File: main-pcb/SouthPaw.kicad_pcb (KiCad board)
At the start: 2 copper layers, 95.5 x 130.5 mm, 68 parts, among them SW1 SW_Push, SW10 SW_Push, SW11 SW_Push, SW12 SW_Push, SW13 SW_Push, SW14 SW_Push, SW15 SW_Push, SW16 SW_Push, SW17 SW_Push, SW18 SW_Push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

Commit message: Making progress
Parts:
- removed L10, L11, logo1, logo3, logo5, logo6, logo7, logo8: LOGO, LOGO
- added STA10: , , F.Cu at (79.0, 134.4)
- added STA9: , , F.Cu at (79.0, 96.3)
- STA1: value 0.91in 128x32 I2C STEMMA QT standoff only -> 0.91in 128x32 I2C STEMMA QT standoff only with cutout; footprint PeteCB:0.91in 128x32 I2C STEMMA QT standoff only -> PeteCB:0.91in 128x32 I2C STEMMA QT standoff only with cutout
- U1: footprint PeteCB:KB2040 through hole hybrid (modified from Elite-C-castellated-24pin-holes) -> PeteCB:KB2040 through hole only (top mount with hotpins 3d model view)
- moved STA3 19.1 mm to (40.9, 96.3)
- moved STA5 19.0 mm to (98.0, 115.4)
- moved STA6 14.7 mm to (114.4, 53.0)
- moved STA7 4.61 mm to (25.4, 54.0)
- moved U1 4.12 mm to (100.7, 39.0), turned to -135 degrees
- moved D3 2.93 mm to (40.8, 41.5)
- moved D8 2.93 mm to (61.6, 41.7)
- moved D4 2.93 mm to (40.8, 31.6)
- moved D6 2.93 mm to (52.2, 26.5)
- moved D9 2.93 mm to (61.6, 31.7)
- moved D1 2.93 mm to (29.1, 26.5)
- moved D10 2.93 mm to (59.1, 31.7)
- moved D2 2.93 mm to (38.3, 41.5)
- moved D5 2.93 mm to (38.3, 31.6)
- moved D7 2.93 mm to (59.1, 41.6)
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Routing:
- net /GND: track 27.6 -> 620.6 mm, vias 21 -> 1
- net /3.3V: track 777.4 -> 498.9 mm, vias 11 -> 6
- net Net-(D5-Pad1): track 118.8 -> 219.7 mm, vias 0 -> 5
- net Net-(RSW1-PadS2): track 150.0 -> 186.0 mm, vias 0 -> 4
- net Net-(D10-Pad2): track 110.9 -> 78.8 mm
- net Net-(SW1-Pad11): track 216.7 -> 184.9 mm, vias 2 -> 1
- net Net-(D25-Pad1): track 155.8 -> 124.0 mm
- net Net-(SW15-Pad22): track 45.4 -> 14.6 mm, vias 1 -> 0
- net Net-(RSW1-PadA): track 124.4 -> 153.0 mm, vias 1 -> 5
- net Net-(D15-Pad1): track 31.0 -> 59.5 mm
- net Net-(D19-Pad1): track 115.3 -> 143.5 mm
- net Net-(RSW1-PadB): track 91.2 -> 118.9 mm, vias 0 -> 2
- net Net-(D8-Pad1): track 77.6 -> 50.5 mm, vias 3 -> 1
- net Net-(SW21-Pad22): track 48.4 -> 22.5 mm, vias 1 -> 0
- net Net-(SW1-Pad24): track 132.4 -> 107.3 mm, vias 4 -> 1
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- removed copper zone on B.Cu, net /GND
- removed copper zone on F.Cu, net /GND
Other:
- board size 95.5 x 130.5 mm -> 99.7 x 136.9 mm
- board text added: "ES 2"

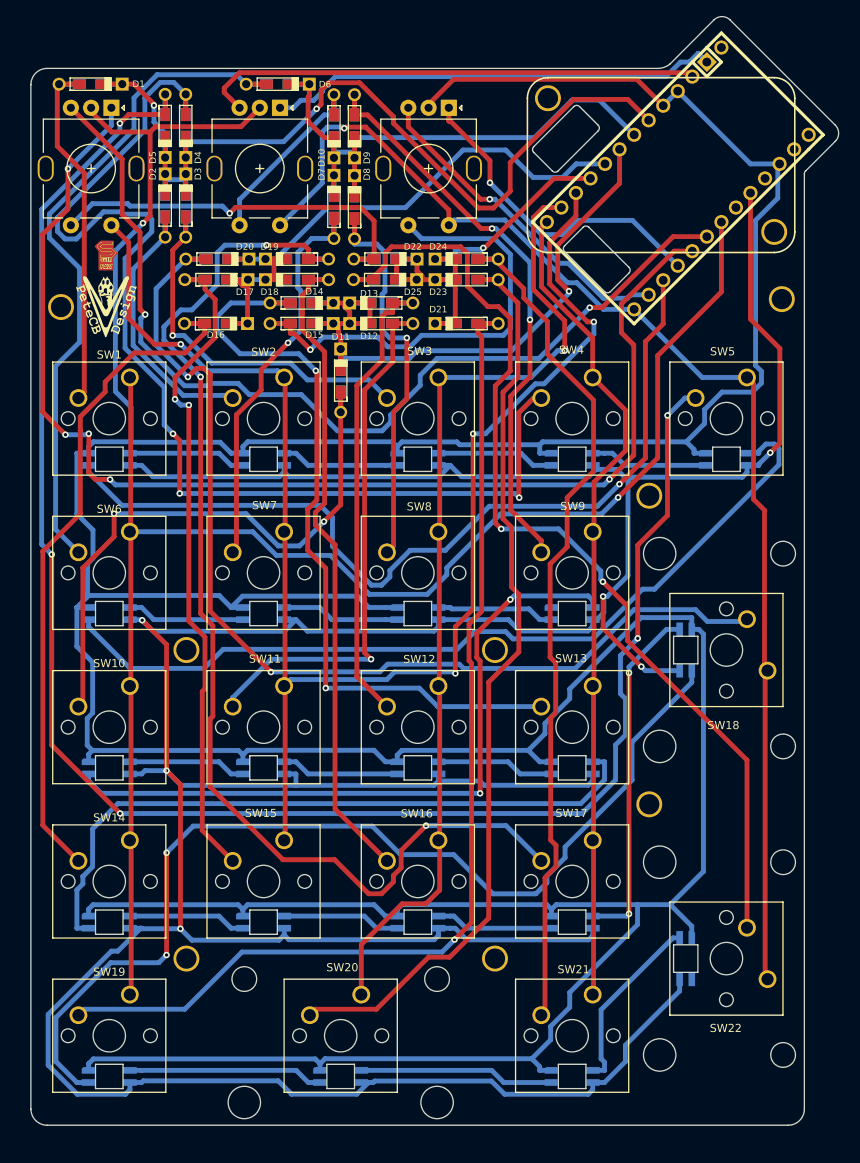
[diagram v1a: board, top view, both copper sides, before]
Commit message: fixed pinnouts
rotary encoders now all share a common a pin
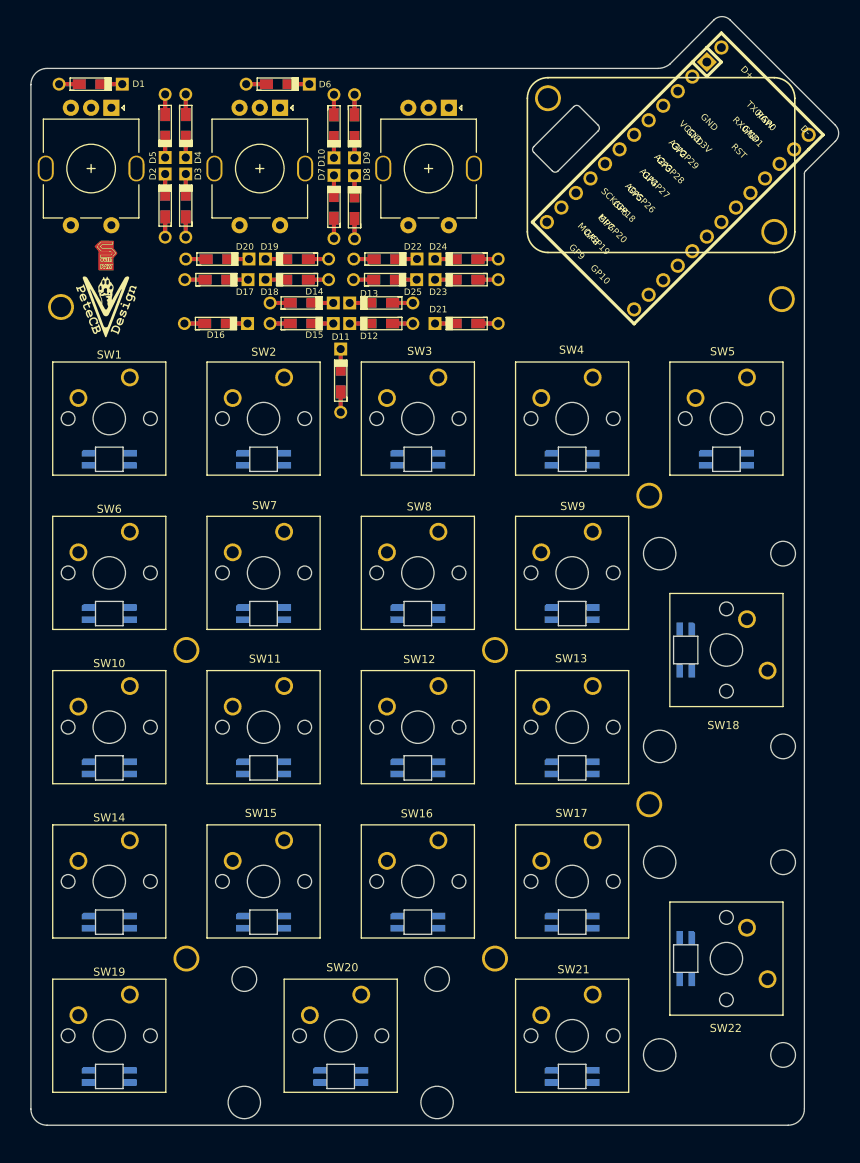
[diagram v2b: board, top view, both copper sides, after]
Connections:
- RSW1 pad A: Net-(RSW1-PadA) -> /ENCA
- RSW2 pad A: Net-(RSW2-PadA) -> /ENCA
- RSW2 pad S2: Net-(RSW2-PadS2) -> Net-(U1-Pad18)
- RSW3 pad A: Net-(RSW3-PadA) -> /ENCA
- RSW3 pad S2: Net-(RSW2-PadS2) -> Net-(U1-Pad18)
- SW1 pad 21: /3.3V -> /RAW
- SW10 pad 21: /3.3V -> /RAW
- SW11 pad 21: /3.3V -> /RAW
- SW12 pad 21: /3.3V -> /RAW
- SW13 pad 21: /3.3V -> /RAW
- SW14 pad 21: /3.3V -> /RAW
- SW15 pad 21: /3.3V -> /RAW
- SW16 pad 21: /3.3V -> /RAW
- SW17 pad 21: /3.3V -> /RAW
- SW18 pad 11: Net-(RSW2-PadS2) -> Net-(U1-Pad18)
- SW18 pad 21: /3.3V -> /RAW
- SW19 pad 21: /3.3V -> /RAW
- SW2 pad 21: /3.3V -> /RAW
- SW20 pad 21: /3.3V -> /RAW
- SW21 pad 21: /3.3V -> /RAW
- SW22 pad 11: Net-(RSW2-PadS2) -> Net-(U1-Pad18)
- SW22 pad 21: /3.3V -> /RAW
- SW3 pad 21: /3.3V -> /RAW
- SW4 pad 21: /3.3V -> /RAW
- SW5 pad 11: Net-(RSW2-PadS2) -> Net-(U1-Pad18)
- SW5 pad 21: /3.3V -> /RAW
- SW6 pad 21: /3.3V -> /RAW
- SW7 pad 21: /3.3V -> /RAW
- SW8 pad 21: /3.3V -> /RAW
- SW9 pad 21: /3.3V -> /RAW
- U1 pad 0: (no net) -> unconnected-(U1-Pad0)
- U1 pad 1: Net-(RSW2-PadA) -> Net-(RSW2-PadB)
- U1 pad 13: Net-(RSW2-PadS2) -> /ENCA
- U1 pad 14: Net-(RSW3-PadB) -> Net-(SW1-Pad24)
- U1 pad 15: Net-(SW1-Pad24) -> unconnected-(U1-Pad15)
- U1 pad 16: Net-(RSW3-PadA) -> unconnected-(U1-Pad16)
- U1 pad 17: Net-(RSW1-PadA) -> unconnected-(U1-Pad17)
- U1 pad 18: Net-(RSW1-PadB) -> Net-(U1-Pad18)
- U1 pad 2: Net-(RSW2-PadB) -> Net-(RSW3-PadB)
- U1 pad 20: unconnected-(U1-Pad20) -> Net-(RSW1-PadB)
- U1 pad 24: unconnected-(U1-Pad24) -> /RAW
- U1 pad 25: (no net) -> unconnected-(U1-Pad25)
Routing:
- net /GND: track 620.6 -> 0.00 mm, vias 1 -> 0
- net /3.3V: track 498.9 -> 0.00 mm, vias 6 -> 0
- net Net-(D5-Pad1): track 219.7 -> 0.00 mm, vias 5 -> 0
- net Net-(RSW1-PadS2): track 186.0 -> 0.00 mm, vias 4 -> 0
- net Net-(SW1-Pad11): track 184.9 -> 0.00 mm, vias 1 -> 0
- net Net-(RSW2-PadS2): track 156.5 -> 0.00 mm, vias 1 -> 0
- net Net-(RSW1-PadA): track 153.0 -> 0.00 mm, vias 5 -> 0
- net Net-(D19-Pad1): track 143.5 -> 0.00 mm, vias 3 -> 0
- net Net-(D4-Pad1): track 140.4 -> 0.00 mm, vias 3 -> 0
- net Net-(D21-Pad1): track 133.5 -> 0.00 mm, vias 1 -> 0
- net Net-(D20-Pad1): track 129.2 -> 0.00 mm, vias 2 -> 0
- net Net-(SW18-Pad22): track 126.0 -> 0.00 mm, vias 2 -> 0
- net Net-(D25-Pad1): track 124.0 -> 0.00 mm, vias 2 -> 0
- net Net-(SW12-Pad11): track 121.3 -> 0.00 mm, vias 1 -> 0
- net Net-(RSW1-PadB): track 118.9 -> 0.00 mm, vias 2 -> 0
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
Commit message: Some work on traces (drc errors present)
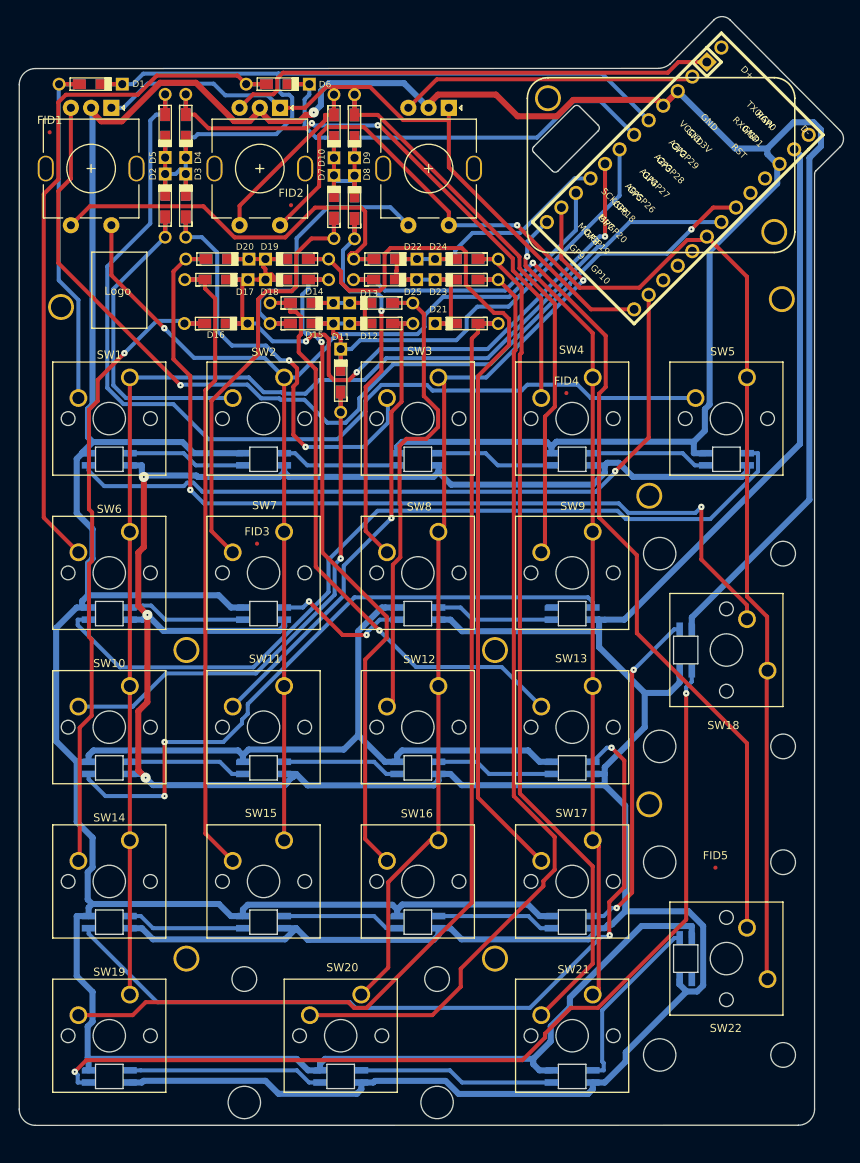
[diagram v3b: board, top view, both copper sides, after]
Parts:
- removed logo0, logo4: LOGO, LOGO
- added FID1: Fiducial, Fiducial:Fiducial_0.5mm_Mask1mm, F.Cu at (24.0, 32.4)
- added FID2: Fiducial, Fiducial:Fiducial_0.5mm_Mask1mm, F.Cu at (53.8, 41.4)
- added FID3: Fiducial, Fiducial:Fiducial_0.5mm_Mask1mm, F.Cu at (49.6, 83.2)
- added FID4: Fiducial, Fiducial:Fiducial_0.5mm_Mask1mm, F.Cu at (87.8, 64.6)
- added FID5: Fiducial, Fiducial:Fiducial_0.5mm_Mask1mm, F.Cu at (106.2, 123.2)
- H1: renamed from STA1; value 0.91in 128x32 I2C STEMMA QT standoff only with cutout -> MountingHole
- H2: renamed from STA7; value (none) -> MountingHole; footprint (none) -> PeteCB:m2.5 hole
- H3: renamed from STA6; value (none) -> MountingHole; footprint (none) -> PeteCB:m2.5 hole
- H4: renamed from STA2; value m2.5 hole -> MountingHole
- H5: renamed from STA3; value (none) -> MountingHole; footprint (none) -> PeteCB:m2.5 hole
- H6: renamed from STA9; value (none) -> MountingHole; footprint (none) -> PeteCB:m2.5 hole
- H7: renamed from STA5; value (none) -> MountingHole; footprint (none) -> PeteCB:m2.5 hole
- H8: renamed from STA4; value (none) -> MountingHole; footprint (none) -> PeteCB:m2.5 hole
- H9: renamed from STA10; value (none) -> MountingHole; footprint (none) -> PeteCB:m2.5 hole
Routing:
- net /GND: track 0.00 -> 662.8 mm, vias 0 -> 1
- net /RAW: track 0.00 -> 517.8 mm, vias 0 -> 3
- net Net-(U1-Pad18): track 0.00 -> 168.1 mm, vias 0 -> 1
- net Net-(SW1-Pad11): track 0.00 -> 158.9 mm
- net Net-(RSW1-PadS2): track 0.00 -> 139.1 mm, vias 0 -> 1
- net Net-(D21-Pad1): track 0.00 -> 131.7 mm
- net Net-(RSW1-PadB): track 0.00 -> 123.6 mm, vias 0 -> 2
- net Net-(D5-Pad1): track 0.00 -> 122.4 mm
- net Net-(D1-Pad2): track 0.00 -> 120.6 mm
- net Net-(D25-Pad1): track 0.00 -> 120.3 mm, vias 0 -> 1
- net Net-(D23-Pad1): track 0.00 -> 120.3 mm
- net Net-(SW18-Pad22): track 0.00 -> 117.4 mm, vias 0 -> 2
- net Net-(D20-Pad1): track 0.00 -> 115.8 mm, vias 0 -> 2
- net Net-(SW12-Pad11): track 0.00 -> 114.3 mm, vias 0 -> 1
- net Net-(D19-Pad1): track 0.00 -> 111.9 mm
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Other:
- board size 99.7 x 136.9 mm -> 101.8 x 136.9 mm
- board text added: "Logo"

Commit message: fixed schematic errors
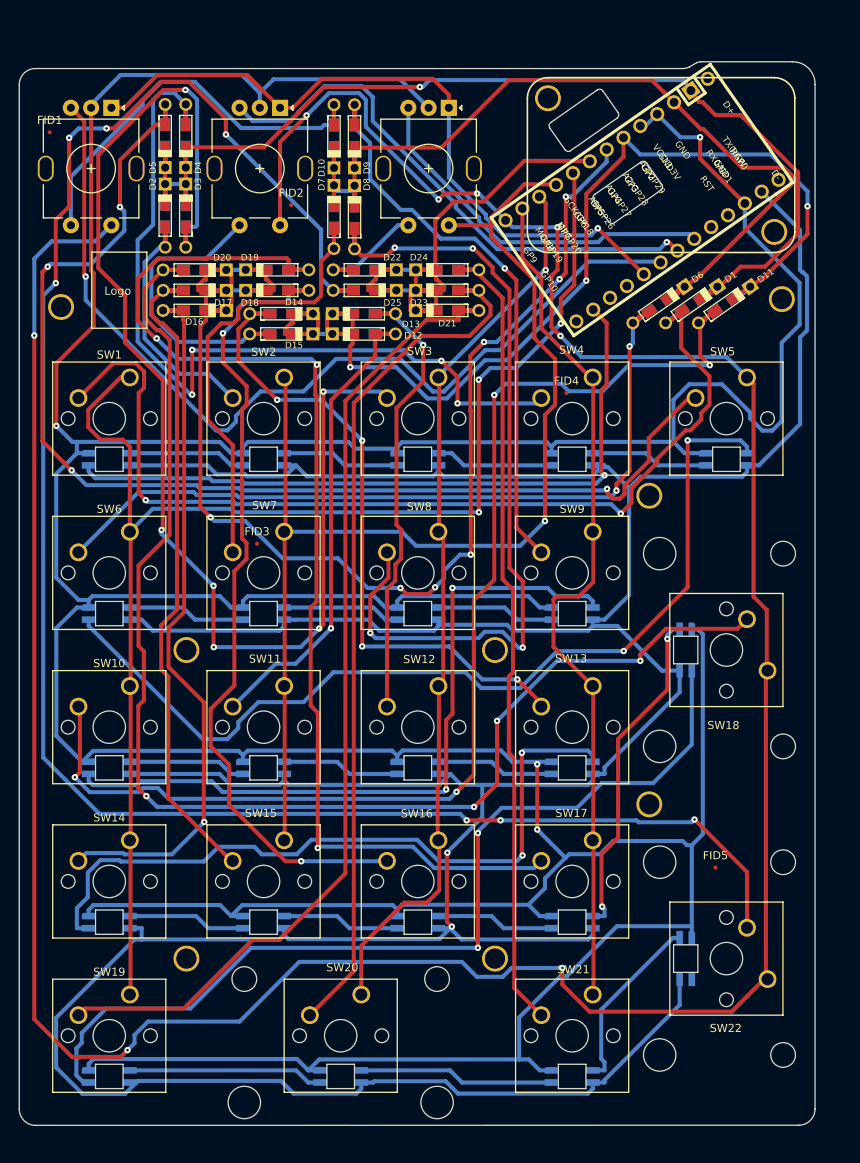
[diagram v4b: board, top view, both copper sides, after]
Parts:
- moved D1 79.0 mm to (103.2, 53.7), turned to 35 degrees
- moved D6 54.4 mm to (99.2, 53.7), turned to 35 degrees
- moved D11 48.3 mm to (107.3, 53.7), turned to 35 degrees
- moved U1 5.19 mm to (96.1, 41.5), turned to -145 degrees
- moved D20 3.11 mm to (41.9, 49.4)
- moved D16 3.09 mm to (41.9, 54.4)
- moved D17 2.99 mm to (41.9, 51.9)
- moved D21 2.88 mm to (73.1, 54.4)
- moved D22 2.88 mm to (62.9, 49.4)
- moved D25 2.84 mm to (62.9, 51.9)
- moved D14 2.84 mm to (52.6, 54.8)
- moved D15 2.82 mm to (52.6, 57.3)
- moved D18 2.78 mm to (52.1, 51.9)
- moved D19 2.78 mm to (52.1, 49.4)
- moved D23 2.73 mm to (73.1, 51.9)
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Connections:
- net /3.3V renamed +3.3V
- net /RAW renamed +5V
- net Net-(SW1-Pad24) renamed /ledDriver
- D1 pad 2: Net-(D1-Pad2) -> /Row1
- D10 pad 2: Net-(D10-Pad2) -> /Row2
- D11 pad 2: Net-(D11-Pad2) -> /Row3
- D12 pad 2: Net-(D11-Pad2) -> /Row3
- D13 pad 2: Net-(D11-Pad2) -> /Row3
- D14 pad 2: Net-(D11-Pad2) -> /Row3
- D15 pad 2: Net-(D11-Pad2) -> /Row3
- D16 pad 2: Net-(D16-Pad2) -> /Row4
- D17 pad 2: Net-(D16-Pad2) -> /Row4
- D18 pad 2: Net-(D16-Pad2) -> /Row4
- D19 pad 2: Net-(D16-Pad2) -> /Row4
- D2 pad 2: Net-(D1-Pad2) -> /Row1
- D20 pad 2: Net-(D16-Pad2) -> /Row4
- D21 pad 2: Net-(D21-Pad2) -> /Row5
- D22 pad 2: Net-(D21-Pad2) -> /Row5
- D23 pad 2: Net-(D21-Pad2) -> /Row5
- D24 pad 2: Net-(D21-Pad2) -> /Row5
- D25 pad 2: Net-(D21-Pad2) -> /Row5
- D3 pad 2: Net-(D1-Pad2) -> /Row1
- D4 pad 2: Net-(D1-Pad2) -> /Row1
- D5 pad 2: Net-(D1-Pad2) -> /Row1
- D6 pad 2: Net-(D10-Pad2) -> /Row2
- D7 pad 2: Net-(D10-Pad2) -> /Row2
- D8 pad 2: Net-(D10-Pad2) -> /Row2
- D9 pad 2: Net-(D10-Pad2) -> /Row2
- RSW1 pad B: Net-(RSW1-PadB) -> /ENC1B
- RSW1 pad C: /GND -> GND
- RSW1 pad S1: Net-(D22-Pad1) -> Net-(D10-Pad1)
- RSW1 pad S2: Net-(RSW1-PadS2) -> /ColE
- RSW2 pad B: Net-(RSW2-PadB) -> /ENC2B
- RSW2 pad C: /GND -> GND
- RSW2 pad S1: Net-(D10-Pad1) -> Net-(D15-Pad1)
- RSW2 pad S2: Net-(U1-Pad18) -> /ColE
- RSW3 pad B: Net-(RSW3-PadB) -> /ENC3B
- RSW3 pad C: /GND -> GND
- RSW3 pad S1: Net-(D15-Pad1) -> Net-(D22-Pad1)
- RSW3 pad S2: Net-(U1-Pad18) -> /ColB
- SW1 pad 11: Net-(SW1-Pad11) -> /ColA
- SW1 pad 23: /GND -> GND
- SW10 pad 11: Net-(SW1-Pad11) -> /ColA
- SW10 pad 23: /GND -> GND
- SW11 pad 11: Net-(RSW1-PadS2) -> /ColB
- SW11 pad 23: /GND -> GND
- SW12 pad 11: Net-(SW12-Pad11) -> /ColC
- SW12 pad 23: /GND -> GND
- SW13 pad 11: Net-(SW13-Pad11) -> /ColD
- SW13 pad 23: /GND -> GND
- SW14 pad 11: Net-(SW1-Pad11) -> /ColA
- SW14 pad 23: /GND -> GND
- SW15 pad 11: Net-(RSW1-PadS2) -> /ColB
- SW15 pad 23: /GND -> GND
- SW16 pad 11: Net-(SW12-Pad11) -> /ColC
- SW16 pad 23: /GND -> GND
- SW17 pad 11: Net-(SW13-Pad11) -> /ColD
- SW17 pad 23: /GND -> GND
- SW18 pad 11: Net-(U1-Pad18) -> /ColE
- SW18 pad 23: /GND -> GND
- SW19 pad 11: Net-(SW1-Pad11) -> /ColA
- SW19 pad 23: /GND -> GND
- SW2 pad 11: Net-(RSW1-PadS2) -> /ColB
- SW2 pad 23: /GND -> GND
- SW20 pad 11: Net-(SW12-Pad11) -> /ColC
- SW20 pad 23: /GND -> GND
- SW21 pad 11: Net-(SW13-Pad11) -> /ColD
- SW21 pad 23: /GND -> GND
- SW22 pad 11: Net-(U1-Pad18) -> /ColE
- SW22 pad 23: /GND -> GND
- SW3 pad 11: Net-(SW12-Pad11) -> /ColC
- SW3 pad 23: /GND -> GND
- SW4 pad 11: Net-(SW13-Pad11) -> /ColD
- SW4 pad 23: /GND -> GND
- SW5 pad 11: Net-(U1-Pad18) -> /ColE
- SW5 pad 23: /GND -> GND
- SW6 pad 11: Net-(SW1-Pad11) -> /ColA
- SW6 pad 23: /GND -> GND
- SW7 pad 11: Net-(RSW1-PadS2) -> /ColB
- SW7 pad 23: /GND -> GND
- SW8 pad 11: Net-(SW12-Pad11) -> /ColC
- SW8 pad 23: /GND -> GND
- SW9 pad 11: Net-(SW13-Pad11) -> /ColD
- SW9 pad 23: unconnected-(SW9-Pad23) -> GND
- U1 pad 1: Net-(RSW2-PadB) -> /Row1
- U1 pad 10: Net-(RSW1-PadS2) -> /ColC
- U1 pad 11: Net-(SW12-Pad11) -> /ColD
- U1 pad 12: Net-(SW13-Pad11) -> /ColE
- U1 pad 13: /ENCA -> unconnected-(U1-Pad13)
- U1 pad 17: unconnected-(U1-Pad17) -> /ENCA
- U1 pad 18: Net-(U1-Pad18) -> /ENC1B
- U1 pad 19: Net-(SW1-Pad11) -> /ENC2B
- U1 pad 2: Net-(RSW3-PadB) -> /Row2
- U1 pad 20: Net-(RSW1-PadB) -> /ENC3B
- U1 pad 23: /GND -> GND
- U1 pad 3: /GND -> GND
- U1 pad 4: /GND -> GND
- U1 pad 5: Net-(D1-Pad2) -> /Row3
- U1 pad 6: Net-(D10-Pad2) -> /Row4
- U1 pad 7: Net-(D11-Pad2) -> /Row5
- U1 pad 8: Net-(D16-Pad2) -> /ColA
- U1 pad 9: Net-(D21-Pad2) -> /ColB
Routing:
- net /GND: track 662.8 -> 0.00 mm, vias 1 -> 0
- net GND: track 0.00 -> 652.9 mm, vias 0 -> 4
- net /ColE: track 0.00 -> 380.6 mm, vias 0 -> 8
- net /ColA: track 0.00 -> 176.1 mm, vias 0 -> 3
- net Net-(U1-Pad18): track 168.1 -> 0.00 mm, vias 1 -> 0
- net /Row4: track 0.00 -> 166.9 mm, vias 0 -> 7
- net Net-(SW1-Pad11): track 158.9 -> 0.00 mm
- net /ColB: track 0.00 -> 147.8 mm, vias 0 -> 1
- net /Row3: track 0.00 -> 140.9 mm, vias 0 -> 3
- net Net-(RSW1-PadS2): track 139.1 -> 0.00 mm, vias 1 -> 0
- net /Row1: track 0.00 -> 136.2 mm, vias 0 -> 1
- net Net-(RSW1-PadB): track 123.6 -> 0.00 mm, vias 2 -> 0
- net Net-(D1-Pad2): track 120.6 -> 0.00 mm
- net /ENC1B: track 0.00 -> 114.6 mm, vias 0 -> 1
- net Net-(SW12-Pad11): track 114.3 -> 0.00 mm, vias 1 -> 0
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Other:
- board size 101.8 x 136.9 mm -> 98.3 x 131.3 mm

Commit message: routing underway
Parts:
- added JPSH1: Jumper_3_Open, Jumper:SolderJumper-3_P2.0mm_Open_TrianglePad1.0x1.5mm, B.Cu at (52.4, 26.3)
- added JPSP2: Jumper_2_Open, Jumper:SolderJumper-2_P1.3mm_Open_TrianglePad1.0x1.5mm, B.Cu at (81.2, 50.8)
- added JPSP3: Jumper_2_Open, Jumper:SolderJumper-2_P1.3mm_Open_TrianglePad1.0x1.5mm, B.Cu at (81.2, 55.4)
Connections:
- RSW1 pad A: /ENCA -> /ENC1A(sharedInSclLedMode)
- RSW2 pad A: /ENCA -> /ENC2A
- RSW3 pad A: /ENCA -> /ENC3A
- U1 pad 15: unconnected-(U1-Pad15) -> Net-(U1-Pad15)
- U1 pad 16: unconnected-(U1-Pad16) -> Net-(U1-Pad16)
- U1 pad 17: /ENCA -> /ENC1A(sharedInSclLedMode)
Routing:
- net GND: track 652.9 -> 0.00 mm, vias 4 -> 0
- net +5V: track 494.3 -> 0.00 mm, vias 2 -> 0
- net /ColE: track 380.6 -> 0.00 mm, vias 8 -> 0
- net Net-(D25-Pad1): track 233.5 -> 0.00 mm, vias 7 -> 0
- net /ColA: track 176.1 -> 0.00 mm, vias 3 -> 0
- net /Row4: track 166.9 -> 0.00 mm, vias 7 -> 0
- net Net-(D20-Pad1): track 164.3 -> 0.00 mm, vias 4 -> 0
- net Net-(D3-Pad1): track 156.5 -> 0.00 mm, vias 6 -> 0
- net Net-(D11-Pad1): track 149.3 -> 0.00 mm, vias 4 -> 0
- net /ColB: track 147.8 -> 0.00 mm, vias 1 -> 0
- net Net-(D5-Pad1): track 145.9 -> 0.00 mm, vias 4 -> 0
- net Net-(D19-Pad1): track 145.2 -> 0.00 mm, vias 3 -> 0
- net /Row3: track 140.9 -> 0.00 mm, vias 3 -> 0
- net /Row1: track 136.2 -> 0.00 mm, vias 1 -> 0
- net Net-(D21-Pad1): track 122.9 -> 0.00 mm
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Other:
- board text added: "Combined -> Encoder A Pins"
- board text added: "^ Seprate ^ Encoder Pins"
